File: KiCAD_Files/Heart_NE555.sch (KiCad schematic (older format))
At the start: 42 parts, among them SW1 SW_DIP_x01, U1 NE555D, U2 4017, U3 4017, U4 4017

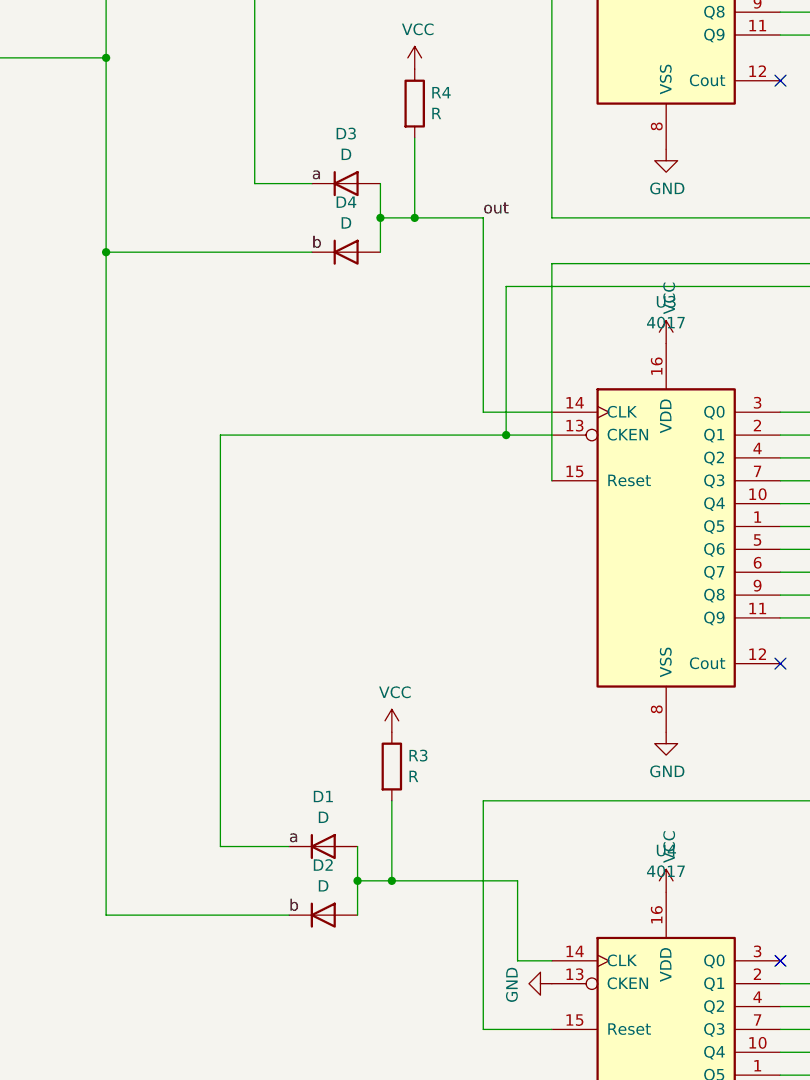
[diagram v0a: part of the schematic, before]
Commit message: fixed an naming error
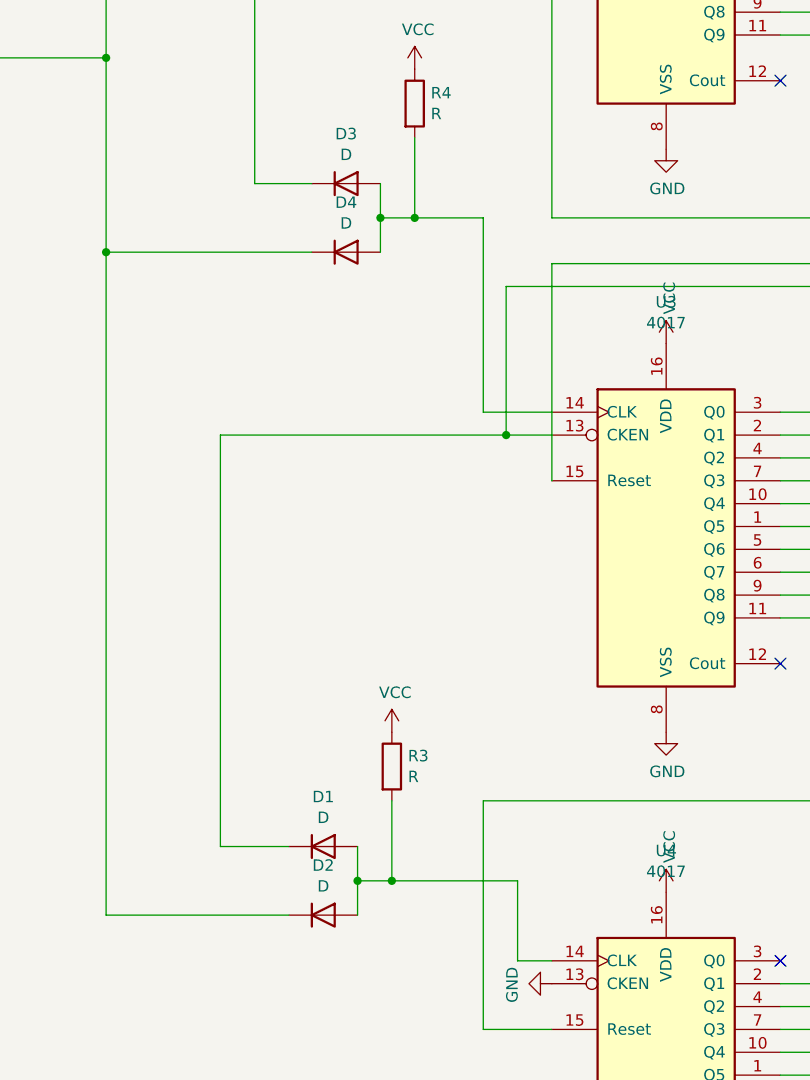
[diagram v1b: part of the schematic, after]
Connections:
- net a: no longer names the net of D3.1 (K), U2.11 (Q9), U2.13 (CKEN)
- net a: no longer D1.1 (K), U3.11 (Q9), U3.13 (CKEN)
- net b: no longer names the net of D2.1 (K), D4.1 (K), U1.3 (Q), U2.14 (CLK)
- net out: no longer names the net of D3.2 (A), D4.2 (A), R4.2, U3.14 (CLK)
- new net: D1.1 (K), U3.11 (Q9), U3.13 (CKEN)
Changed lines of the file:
@@
 Wire Wire Line
 	5900 4300 5750 4300
-Text Label 6200 4300 0    50   ~ 0
-out
-Text Label 5450 4150 0    50   ~ 0
-a
-Text Label 5450 4450 0    50   ~ 0
-b
 $Comp
 L power:VCC #PWR010
@@
 Wire Wire Line
 	5800 7200 5650 7200
-Text Label 5350 7050 0    50   ~ 0
-a
-Text Label 5350 7350 0    50   ~ 0
-b
 $Comp
 L power:VCC #PWR014

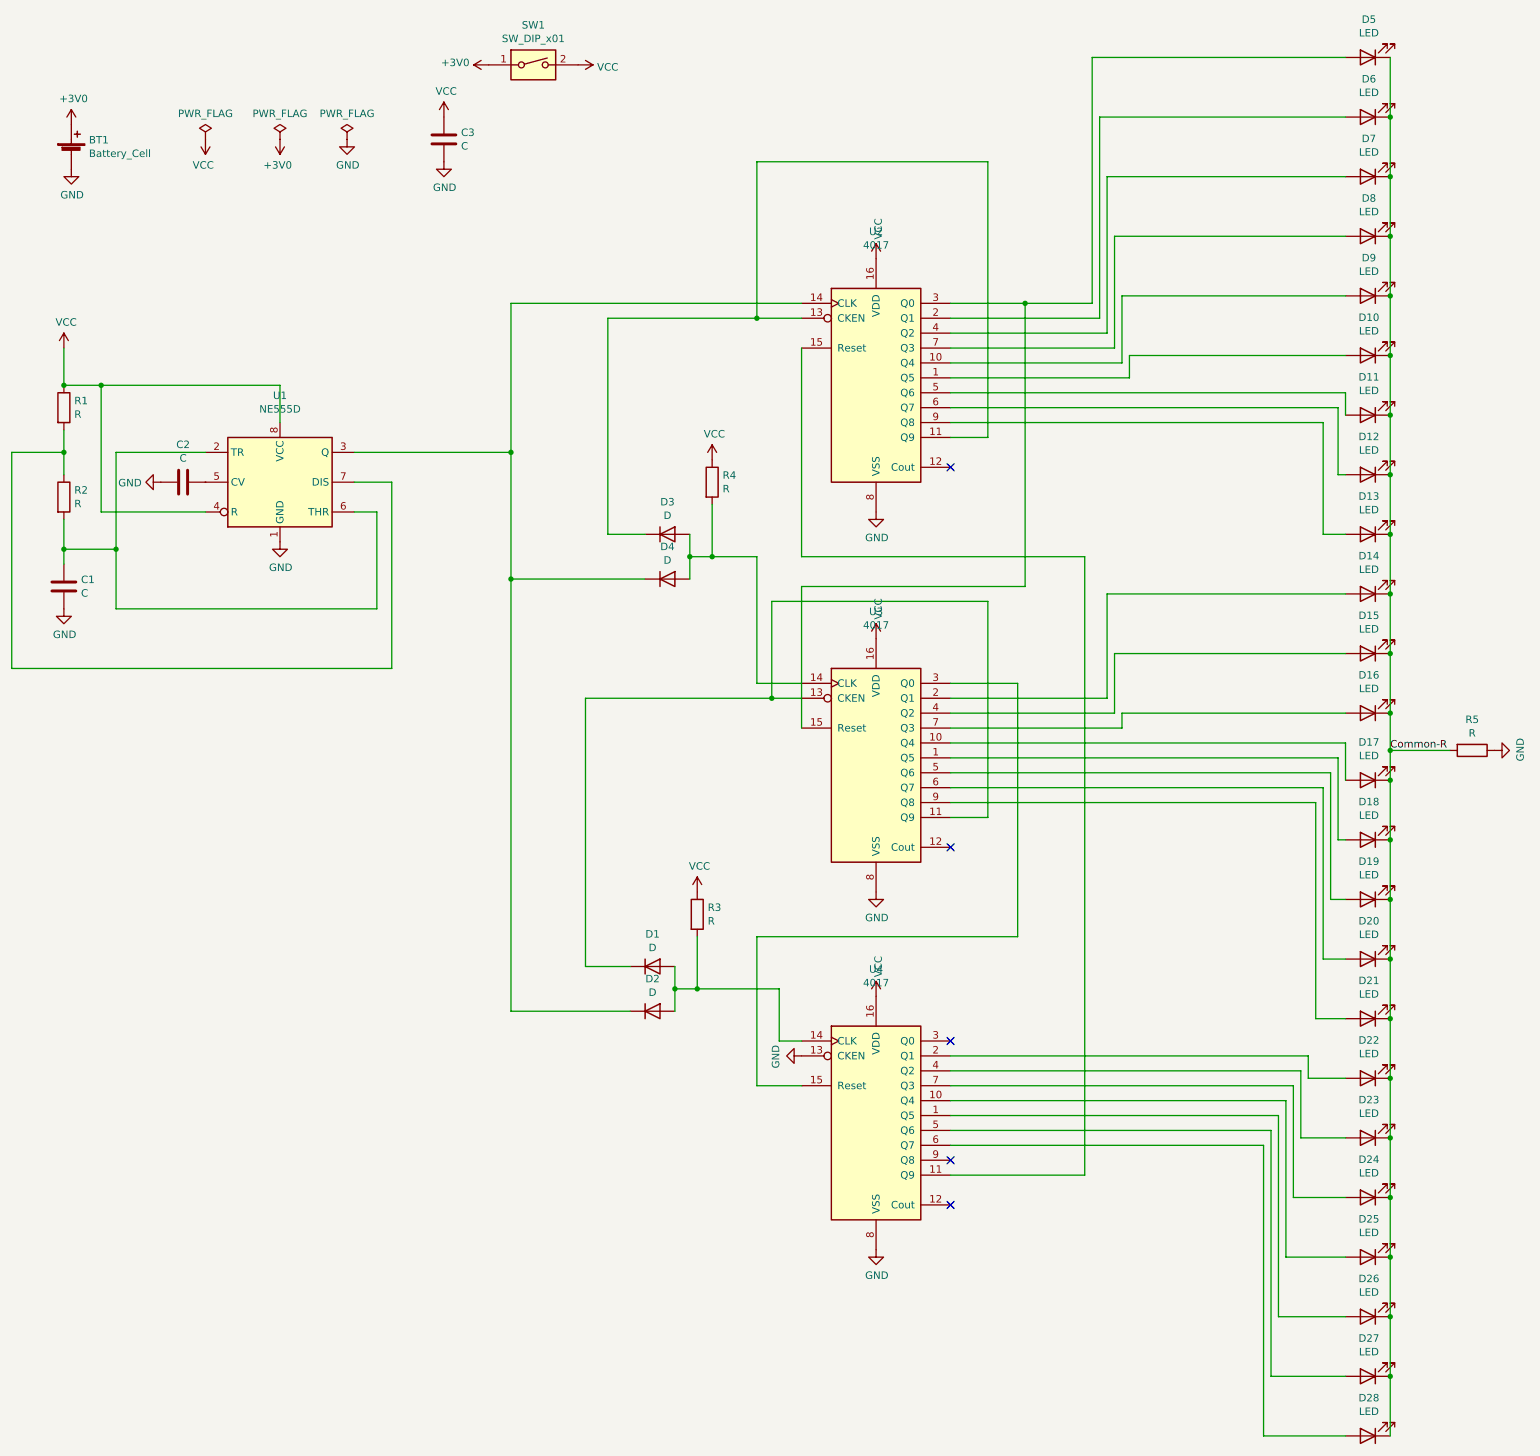
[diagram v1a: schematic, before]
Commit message: changed footprints of diodes, fixed last-led-bug
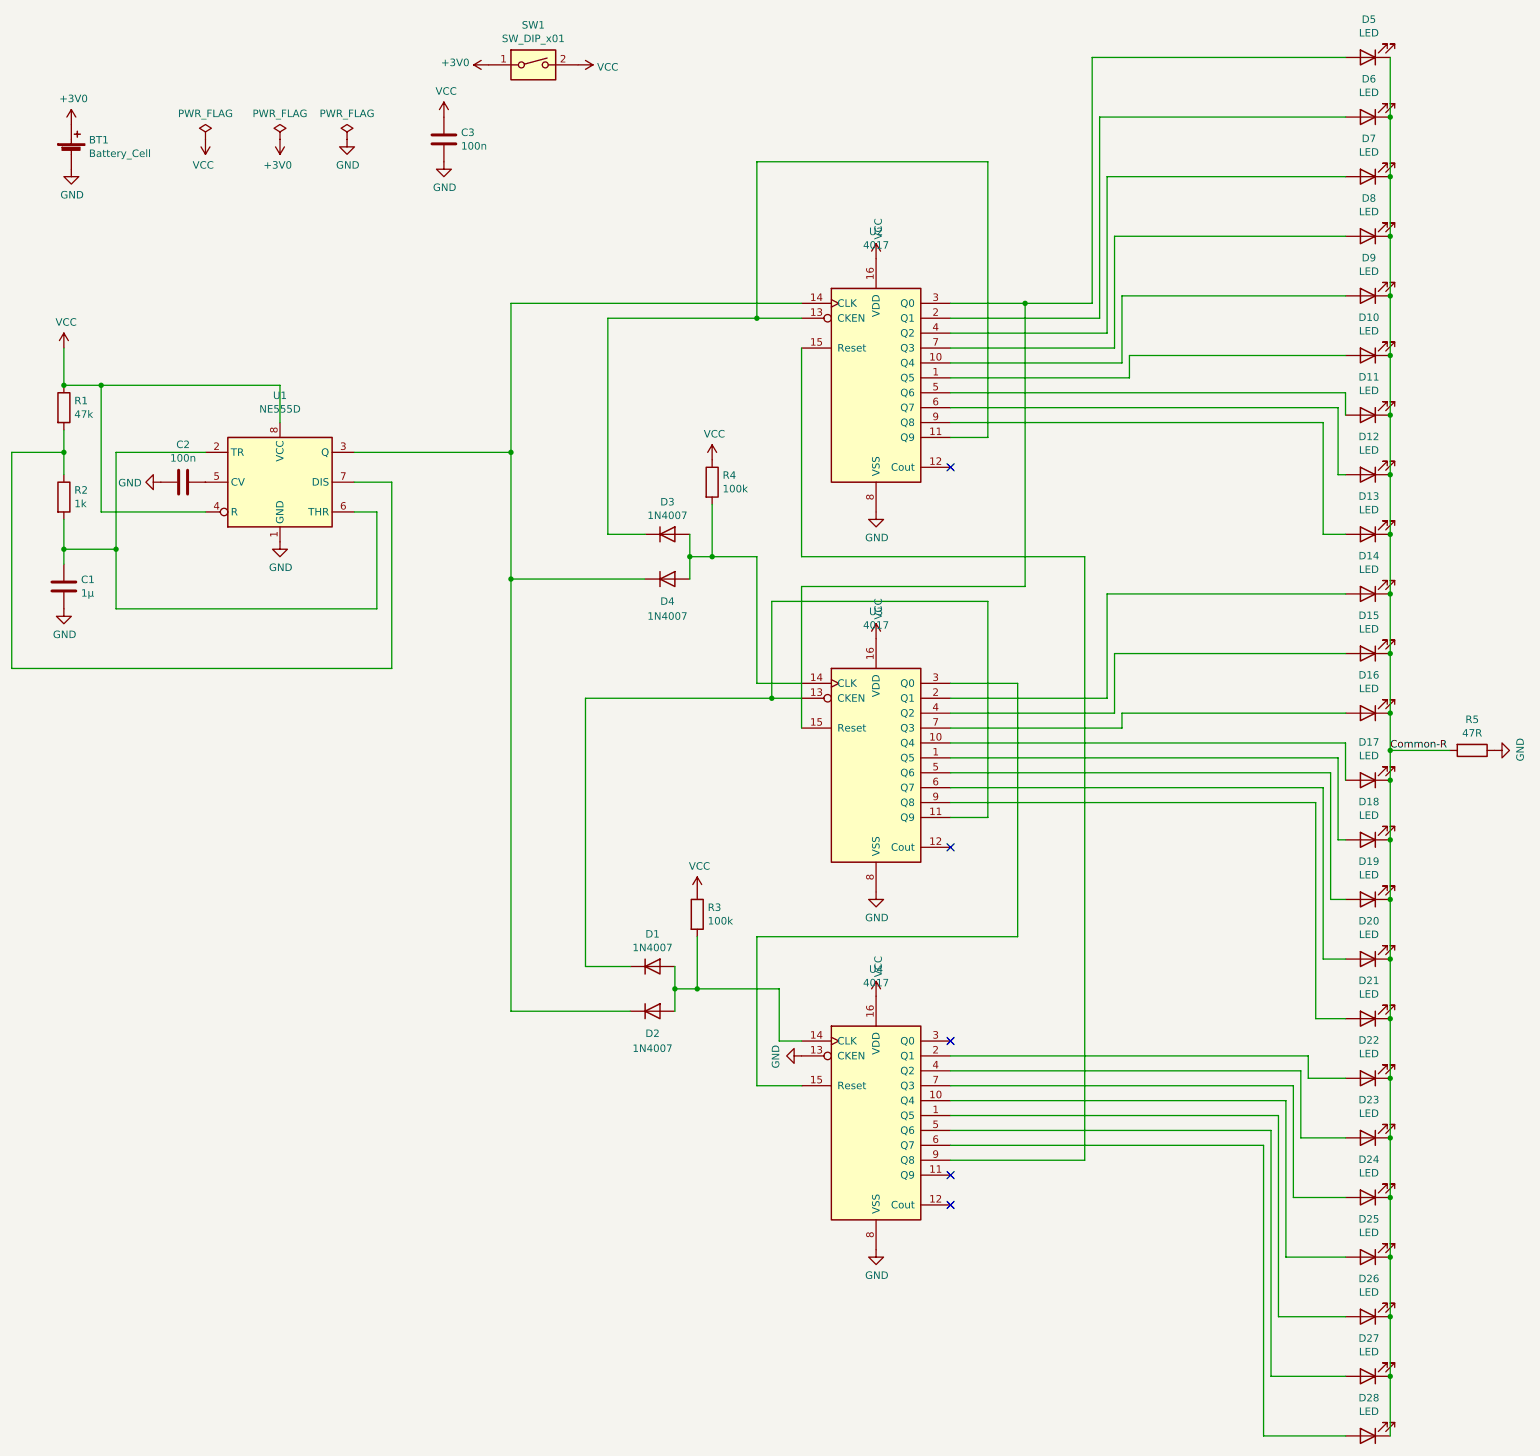
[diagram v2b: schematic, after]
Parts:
- C1: value C -> 1µ
- C2, C3: value C -> 100n
- D1, D2, D3, D4: value D -> 1N4007; footprint Diode_SMD:D_0805_2012Metric_Pad1.15x1.40mm_HandSolder -> Diode_SMD:D_SOD-123
- R1: value R -> 47k
- R2: value R -> 1k
- R3, R4: value R -> 100k
- R5: value R -> 47R
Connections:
- net at U2.15 (Reset): now also U4.9 (Q8); no longer U4.11 (Q9)
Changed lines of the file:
@@
 P 4100 1500
 F 0 "C3" H 4215 1546 50  0000 L CNN
-F 1 "C" H 4215 1455 50  0000 L CNN
+F 1 "100n" H 4215 1455 50  0000 L CNN
 F 2 "Capacitor_SMD:C_0805_2012Metric_Pad1.18x1.45mm_HandSolder" H 4138 1350 50  0001 C CNN
 F 3 "~" H 4100 1500 50  0001 C CNN
@@
 P 1550 3300
 F 0 "R1" H 1620 3346 50  0000 L CNN
-F 1 "R" H 1620 3255 50  0000 L CNN
+F 1 "47k" H 1620 3255 50  0000 L CNN
 F 2 "Resistor_SMD:R_0805_2012Metric_Pad1.20x1.40mm_HandSolder" V 1480 3300 50  0001 C CNN
 F 3 "~" H 1550 3300 50  0001 C CNN
@@
 P 1550 3900
 F 0 "R2" H 1620 3946 50  0000 L CNN
-F 1 "R" H 1620 3855 50  0000 L CNN
+F 1 "1k" H 1620 3855 50  0000 L CNN
 F 2 "Resistor_SMD:R_0805_2012Metric_Pad1.20x1.40mm_HandSolder" V 1480 3900 50  0001 C CNN
 F 3 "~" H 1550 3900 50  0001 C CNN
@@
 P 1550 4500
 F 0 "C1" H 1665 4546 50  0000 L CNN
-F 1 "C" H 1665 4455 50  0000 L CNN
+F 1 "1µ" H 1665 4455 50  0000 L CNN
 F 2 "Capacitor_SMD:C_0805_2012Metric_Pad1.18x1.45mm_HandSolder" H 1588 4350 50  0001 C CNN
 F 3 "~" H 1550 4500 50  0001 C CNN
@@
 P 2350 3800
 F 0 "C2" V 2098 3800 50  0000 C CNN
-F 1 "C" V 2189 3800 50  0000 C CNN
+F 1 "100n" V 2189 3800 50  0000 C CNN
 F 2 "Capacitor_SMD:C_0805_2012Metric_Pad1.18x1.45mm_HandSolder" H 2388 3650 50  0001 C CNN
 F 3 "~" H 2350 3800 50  0001 C CNN
@@
 P 5600 4150
 F 0 "D3" H 5600 4367 50  0000 C CNN
-F 1 "D" H 5600 4276 50  0000 C CNN
-F 2 "Diode_SMD:D_0805_2012Metric_Pad1.15x1.40mm_HandSolder" H 5600 4150 50  0001 C CNN
+F 1 "1N4007" H 5600 4276 50  0000 C CNN
+F 2 "Diode_SMD:D_SOD-123" H 5600 4150 50  0001 C CNN
 F 3 "~" H 5600 4150 50  0001 C CNN
 	1    5600 4150
@@
 U 1 1 60072854
 P 5600 4450
-F 0 "D4" H 5600 4667 50  0000 C CNN
-F 1 "D" H 5600 4576 50  0000 C CNN
-F 2 "Diode_SMD:D_0805_2012Metric_Pad1.15x1.40mm_HandSolder" H 5600 4450 50  0001 C CNN
+F 0 "D4" H 5600 4300 50  0000 C CNN
+F 1 "1N4007" H 5600 4200 50  0000 C CNN
+F 2 "Diode_SMD:D_SOD-123" H 5600 4450 50  0001 C CNN
 F 3 "~" H 5600 4450 50  0001 C CNN
 	1    5600 4450
@@
 P 5900 3800
 F 0 "R4" H 5970 3846 50  0000 L CNN
-F 1 "R" H 5970 3755 50  0000 L CNN
+F 1 "100k" H 5970 3755 50  0000 L CNN
 F 2 "Resistor_SMD:R_0805_2012Metric_Pad1.20x1.40mm_HandSolder" V 5830 3800 50  0001 C CNN
 F 3 "~" H 5900 3800 50  0001 C CNN
@@
 P 5500 7050
 F 0 "D1" H 5500 7267 50  0000 C CNN
-F 1 "D" H 5500 7176 50  0000 C CNN
-F 2 "Diode_SMD:D_0805_2012Metric_Pad1.15x1.40mm_HandSolder" H 5500 7050 50  0001 C CNN
+F 1 "1N4007" H 5500 7176 50  0000 C CNN
+F 2 "Diode_SMD:D_SOD-123" H 5500 7050 50  0001 C CNN
 F 3 "~" H 5500 7050 50  0001 C CNN
 	1    5500 7050
@@
 U 1 1 6007C190
 P 5500 7350
-F 0 "D2" H 5500 7567 50  0000 C CNN
-F 1 "D" H 5500 7476 50  0000 C CNN
-F 2 "Diode_SMD:D_0805_2012Metric_Pad1.15x1.40mm_HandSolder" H 5500 7350 50  0001 C CNN
+F 0 "D2" H 5500 7200 50  0000 C CNN
+F 1 "1N4007" H 5500 7100 50  0000 C CNN
+F 2 "Diode_SMD:D_SOD-123" H 5500 7350 50  0001 C CNN
 F 3 "~" H 5500 7350 50  0001 C CNN
 	1    5500 7350
@@
 P 5800 6700
 F 0 "R3" H 5870 6746 50  0000 L CNN
-F 1 "R" H 5870 6655 50  0000 L CNN
+F 1 "100k" H 5870 6655 50  0000 L CNN
 F 2 "Resistor_SMD:R_0805_2012Metric_Pad1.20x1.40mm_HandSolder" V 5730 6700 50  0001 C CNN
 F 3 "~" H 5800 6700 50  0001 C CNN
@@
 $EndComp
 Wire Wire Line
-	7500 8450 8400 8450
-Wire Wire Line
-	8400 8450 8400 4300
-Wire Wire Line
 	8400 4300 6500 4300
 Wire Wire Line
@@
 P 11000 5600
 F 0 "R5" V 10793 5600 50  0000 C CNN
-F 1 "R" V 10884 5600 50  0000 C CNN
+F 1 "47R" V 10884 5600 50  0000 C CNN
 F 2 "Resistor_SMD:R_0805_2012Metric_Pad1.20x1.40mm_HandSolder" V 10930 5600 50  0001 C CNN
 F 3 "~" H 11000 5600 50  0001 C CNN
@@
 	9600 10200 10150 10200
 NoConn ~ 7500 7550
-NoConn ~ 7500 8350
 Text Label 10450 5600 0    50   ~ 0
 Common-R
+Wire Wire Line
+	7500 8350 8400 8350
+Wire Wire Line
+	8400 8350 8400 4300
+NoConn ~ 7500 8450
 $EndSCHEMATC
